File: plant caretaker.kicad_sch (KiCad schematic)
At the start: 1 part, among them U4 ESP32-C3

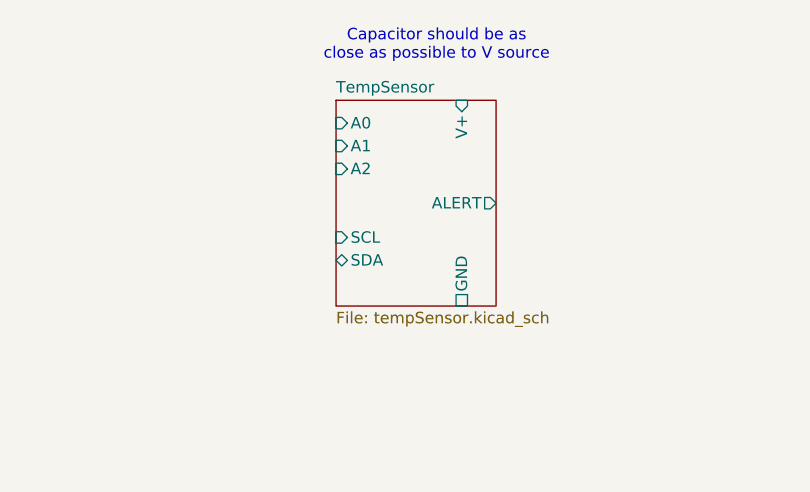
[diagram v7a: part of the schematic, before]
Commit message: Cleanup temperature sensor
Reconnected grounds and removed useless pins
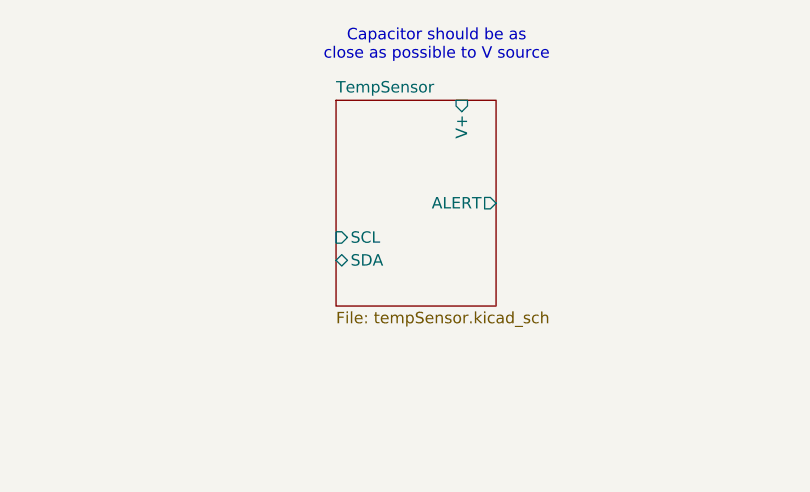
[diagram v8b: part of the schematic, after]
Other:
- sheet TempSensor ports: added none; removed A0, A1, A2, GND
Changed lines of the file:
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@@
-			)
-		)
-		(pin "A1" input
-			(at 142.24 44.45 180)
-			(effects
-				(font
-					(size 1.27 1.27)
-				)
-				(justify left)
-			)
-		)
-		(pin "A0" input
-			(at 142.24 41.91 180)
-			(effects
-				(font
-					(size 1.27 1.27)
-				)
-				(justify left)
 			)
 		)
 		(pin "SCL" input
 			(at 142.24 54.61 180)
-			(effects
-				(font
-					(size 1.27 1.27)
-				)
-				(justify left)
-			)
-		)
-		(pin "A2" input
-			(at 142.24 46.99 180)
 			(effects
 				(font
@@
 			)
 		)
-		(pin "GND" passive
-			(at 156.21 62.23 270)
-			(effects
-				(font
-					(size 1.27 1.27)
-				)
-				(justify left)
-			)
-		)
